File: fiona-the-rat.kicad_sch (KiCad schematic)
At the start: 65 parts, among them J1 USB_TP_P, J10 ~{CHG}_TP, J11 +1V1_TP, J12 VBAT_TP, J13 +3V3_TP, J14 SWD, J19 GPIO0, J2 USB_TP_N, J20 GPIO1, J21 GPIO2, J22 Haptics, J3 XTAL_TP, J4 USB_C_Receptacle_PowerOnly_6P, J5 VBAT_ADC_TP, J6 Periph, J7 GND_TP_1, J8 GND_TP_2, J9 GND_TP_3, Q1 MMBT2222A, SW1 1825027-8, U1 RP2040, U3 W25Q128JVSIQ, U4 BQ21040DBVR, U5 AP2112K-3.3, Y2 ABM8G-12.000MHZ-18-D2Y-T

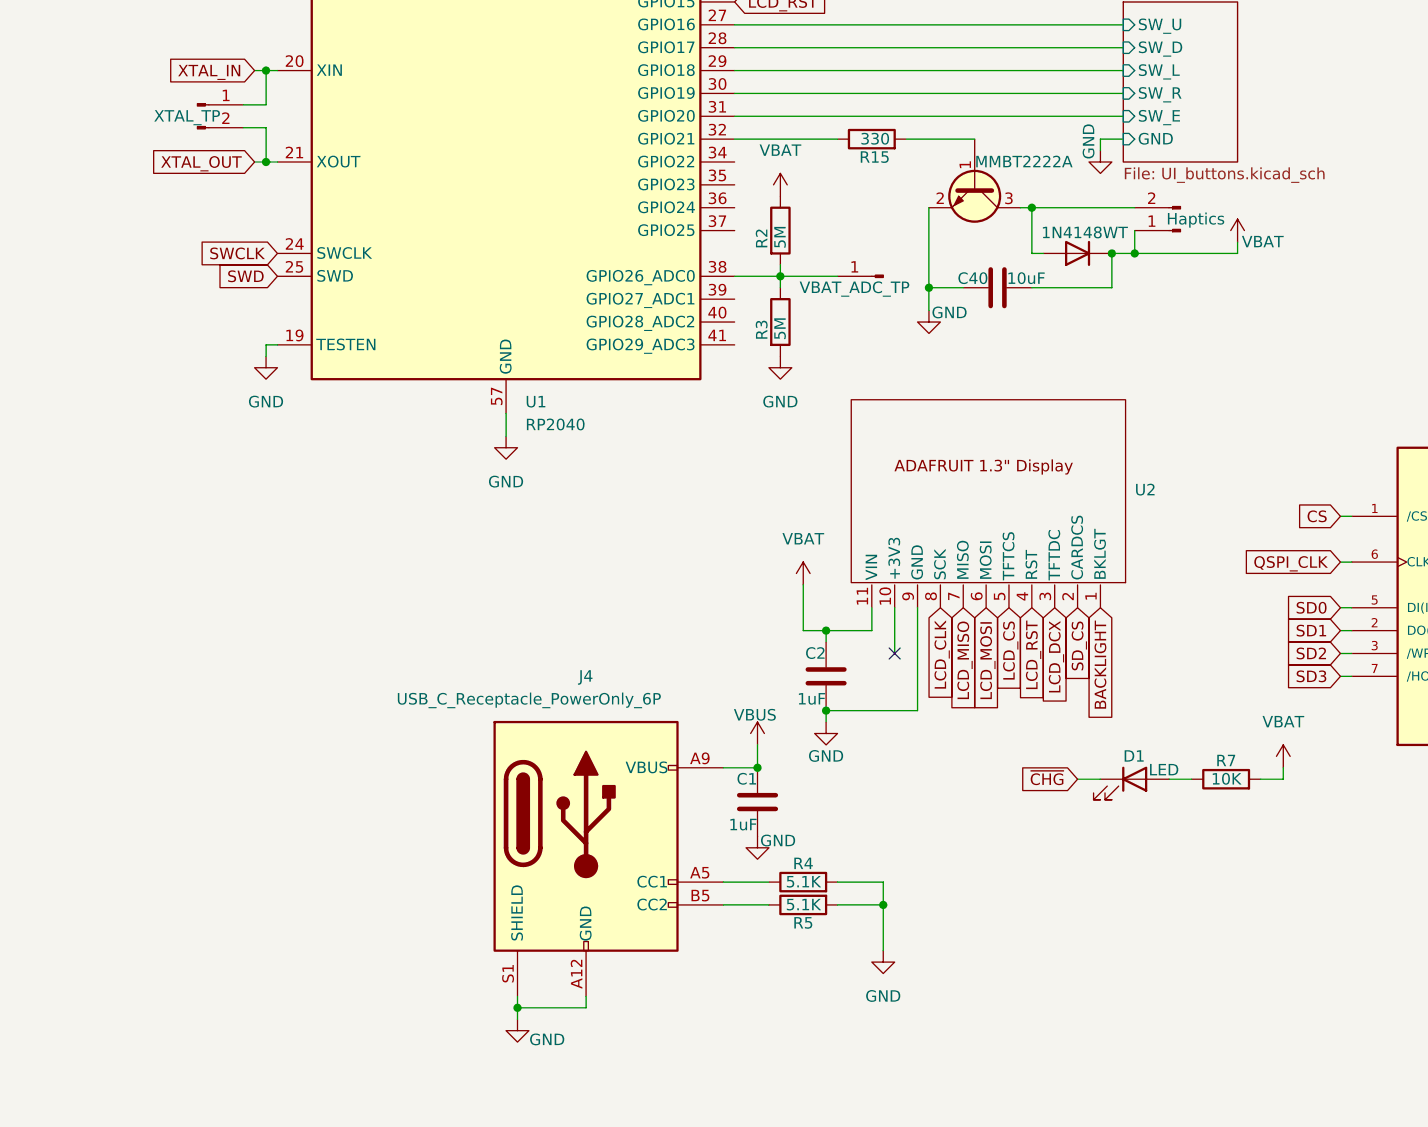
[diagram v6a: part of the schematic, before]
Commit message: Add curr. sense to scheme
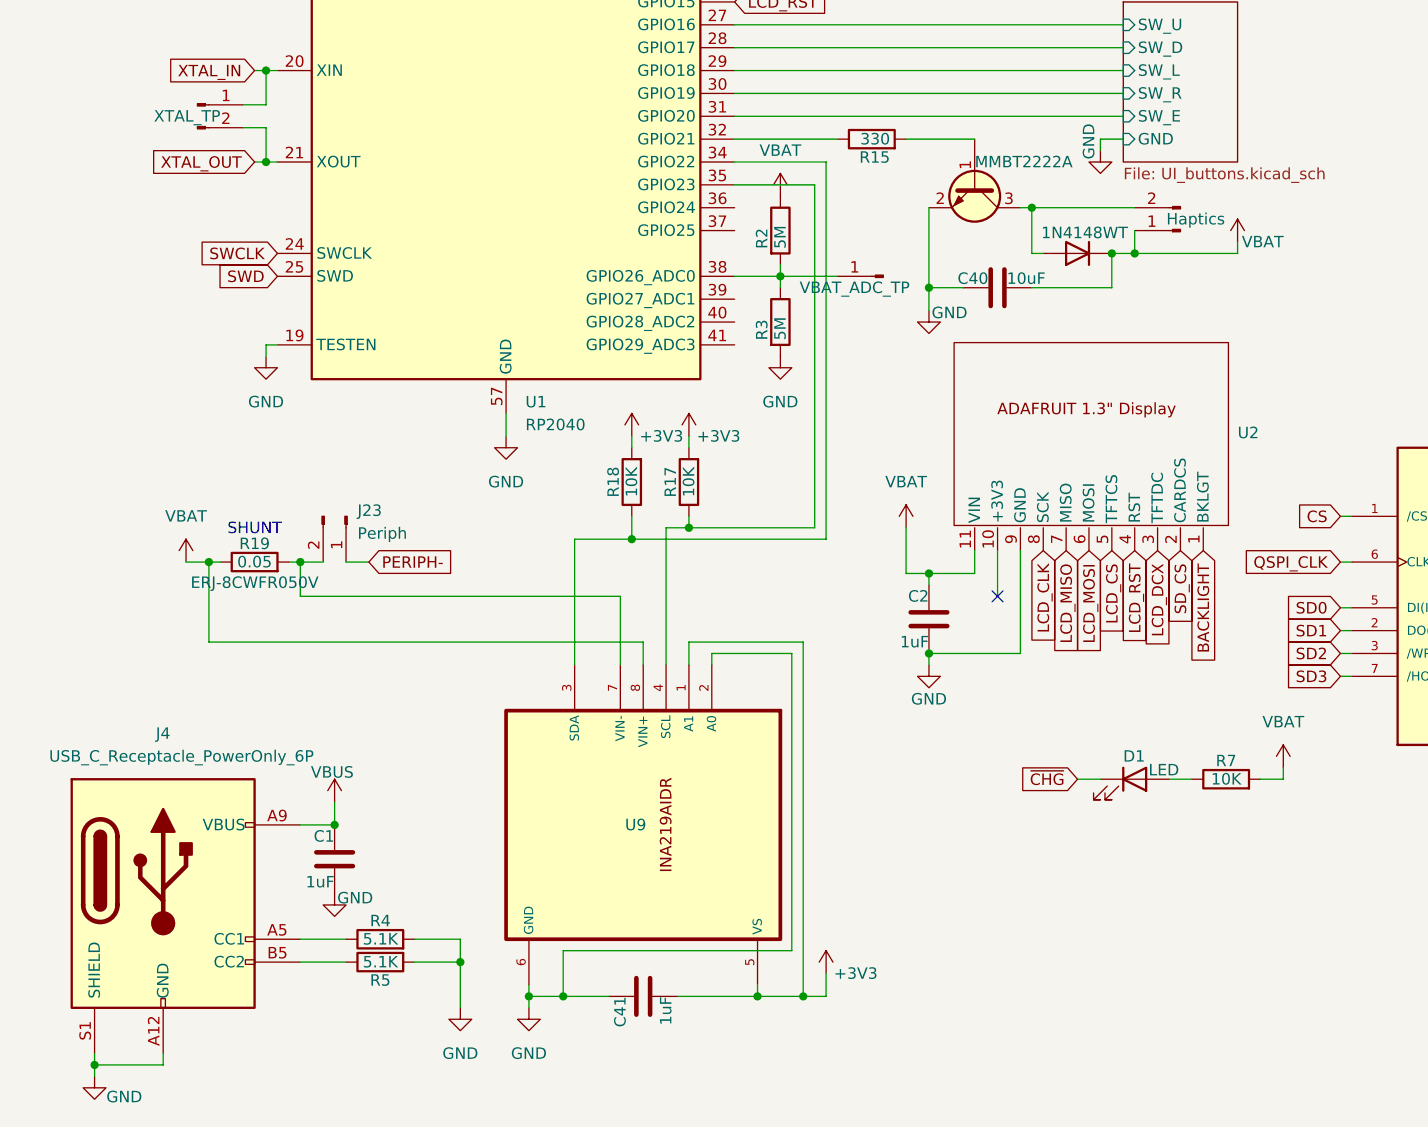
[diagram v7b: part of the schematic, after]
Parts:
- added C41: 1uF, Capacitor_SMD:C_0603_1608Metric, symbol Device:C
- added J23: Periph, Connector_JST:JST_XH_B2B-XH-A_1x02_P2.50mm_Vertical, symbol Connector:Conn_01x02_Pin
- added R17, R18: 10K, Resistor_SMD:R_0603_1608Metric, symbol Device:R
- added R19: 0.05, PCM_Resistor_SMD_AKL:R_1206_3216Metric, symbol Device:R
- added U9: ~, pfornage-kicad-lib:INA219AIDR, symbol pfornage-kicad-lib:INA219AIDR
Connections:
- net +3V3: now also C41.2, R17.2, R18.2, U9.1 (A1), U9.5 (VS)
- net GND: now also C41.1, U9.2 (A0), U9.6 (GND)
- net VBAT: now also R19.1, U9.8 (VIN+)
- net at U1.34 (GPIO22): now also R18.1, U9.3 (SDA)
- net at U1.35 (GPIO23): now also R17.1, U9.4 (SCL)
- new net: J23.2 (Pin_2), R19.2, U9.7 (VIN-)
- new net PERIPH-: J23.1 (Pin_1)
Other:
- note added: "SHUNT"
- moved on the sheet: C1, C2, J4, R4, R5, U2
